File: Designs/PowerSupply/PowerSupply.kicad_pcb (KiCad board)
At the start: 2 copper layers, 101.6 x 86.4 mm, 14 parts, among them J1 Out, U1 L7812, U2 L7912

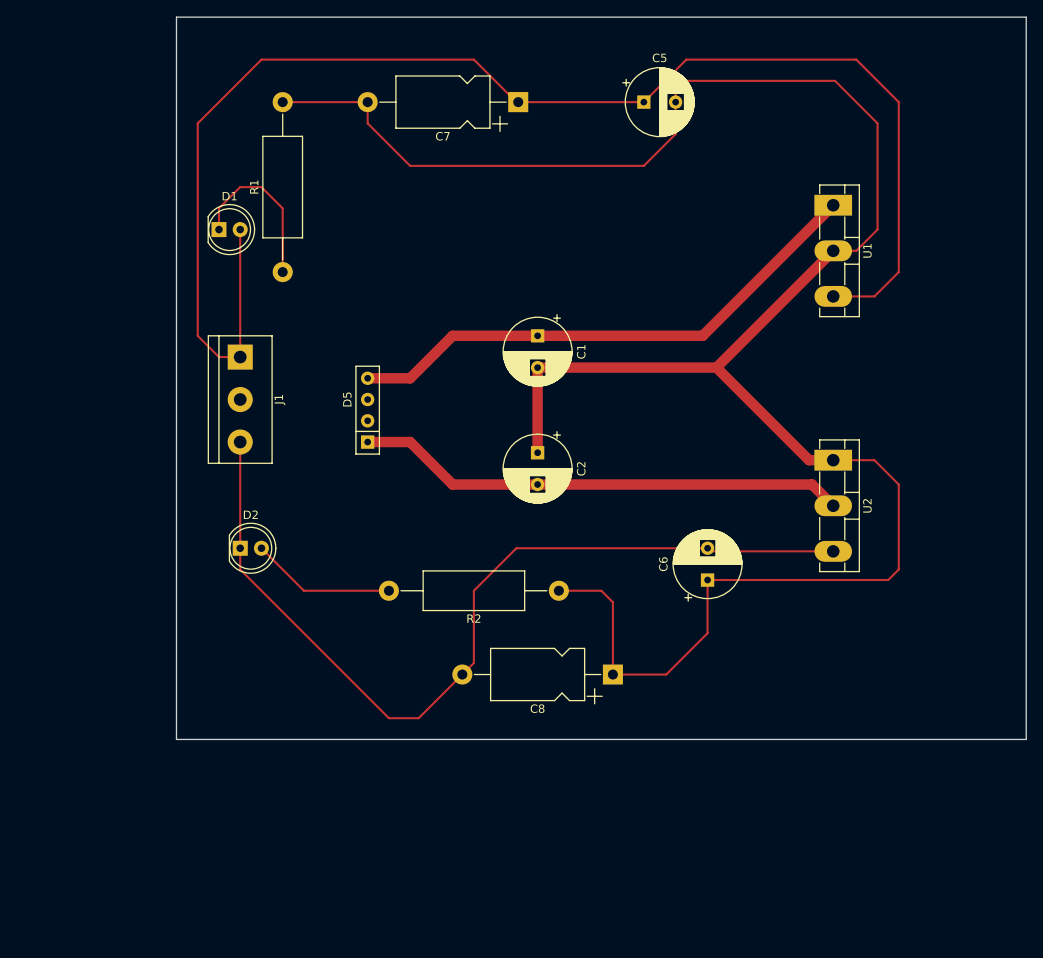
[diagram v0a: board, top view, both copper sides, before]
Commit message: update powersupply design
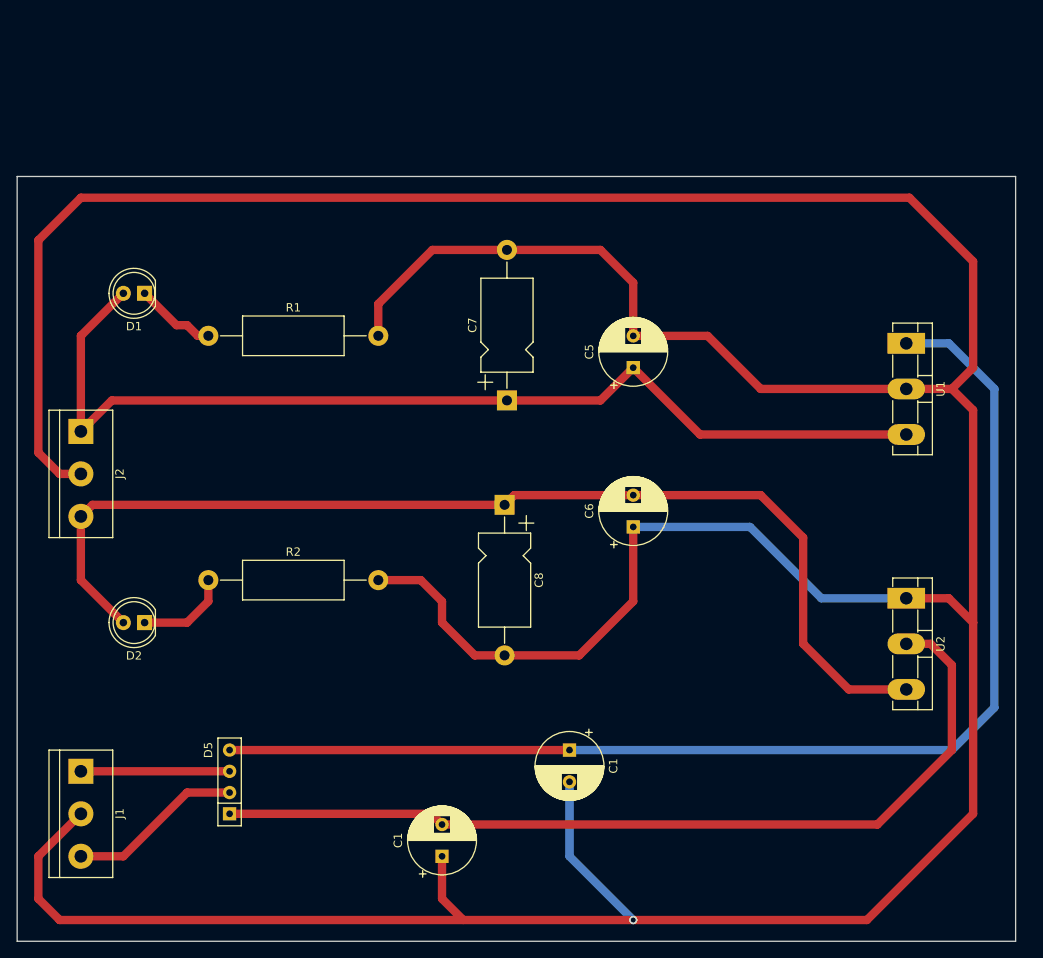
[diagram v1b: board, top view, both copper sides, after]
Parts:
- removed the C1 at (152.4, 66.0)
- removed C2: 2200uf/35V, Capacitor_THT:CP_Radial_D8.0mm_P3.80mm
- added C1: 2200uf/35V, Capacitor_THT:CP_Radial_D8.0mm_P3.80mm, F.Cu at (156.2, 115.6)
- added C1: 2200uf/35V, Capacitor_THT:CP_Radial_D8.0mm_P3.80mm, F.Cu at (141.0, 128.3)
- added J2: Out, TerminalBlock:TerminalBlock_bornier-3_P5.08mm, F.Cu at (97.8, 77.5)
- J1: value Out -> In
- moved J1 53.1 mm to (97.8, 118.1)
- moved D5 47.4 mm to (115.6, 123.2)
- moved R2 41.9 mm to (113.0, 95.2), turned to 0 degrees
- moved C7 35.7 mm to (148.7, 73.8), turned to 90 degrees
- moved C5 31.8 mm to (163.8, 69.8), turned to 90 degrees
- moved C8 24.1 mm to (148.4, 86.2), turned to -90 degrees
- moved U2 18.7 mm to (196.5, 97.4)
- moved U1 18.7 mm to (196.5, 66.9)
- moved D2 14.5 mm to (105.4, 100.3), turned to 180 degrees
- moved R1 11.7 mm to (113.0, 66.0), turned to 0 degrees
- moved D1 11.7 mm to (105.4, 61.0), turned to 180 degrees
- moved C6 10.9 mm to (163.8, 88.9)
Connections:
- C8 pad 1: GND -> Net-(D2-K)
- C8 pad 2: Net-(D2-K) -> GND
- D2 pad 1: Net-(D2-K) -> Net-(D2-A)
- D2 pad 2: Net-(D2-A) -> Net-(D2-K)
- J1 pad 1: Net-(D1-A) -> Net-(T1-SA)
- J1 pad 3: Net-(D2-K) -> Net-(T1-SB)
- R2 pad 1: GND -> Net-(D2-A)
- R2 pad 2: Net-(D2-A) -> GND
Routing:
- net GND: track 255.9 -> 553.7 mm, vias 0 -> 1
- net Net-(D5-+): track 64.2 -> 144.4 mm
- net Net-(D5--): track 58.8 -> 107.2 mm
- net Net-(D1-A): track 169.4 -> 123.8 mm
- net Net-(D2-K): track 107.1 -> 131.6 mm
- net Net-(T1-SB): track 0.00 -> 20.9 mm
- net Net-(T1-SA): track 0.00 -> 17.8 mm
- net Net-(D1-K): track 19.9 -> 9.72 mm
- net Net-(D2-A): track 17.3 -> 11.2 mm
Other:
- board size 101.6 x 86.4 mm -> 119.4 x 91.4 mm
